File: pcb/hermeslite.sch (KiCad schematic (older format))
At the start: 68 parts, among them CN1 MEC6-140_CONNECTOR_BEMICRO, CN2 PCIE, P1 DIL20, P15 61.440, P16 DIPSW, P2 CONN_15, P24 BNC, P25 BNC, P3 CONN_1, P4 CONN_1, P5 CONN_1, P6 CONN_1, P7 CONN_1, T1 8:1, T3 4:1, U1 AD9866BCPZ

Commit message: RTL cleanup and upgrade to Quartus 14.0
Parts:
- C1, C10, C11, C12, C13, C14, C15, C16, C17, C18, C2, C21, C23, C24, C26, C27, C28, C29, C3, C30, C4, C5, C6, C7, C8, C9, R2, R3, R4, R5, R6, R7: footprint (none) -> SMD_Packages:SM0805
- C19, C20, C22: footprint (none) -> SMD_Packages:SM1206POL
- C25: footprint (none) -> SMD_Packages:SM1206
- C31, C32, R8, R9: footprint (none) -> SMD_Packages:SMD-0805
- CN1: footprint (none) -> HERMESLITE:MEC6-140-02-X-D-RAX
- CN2: footprint (none) -> HERMESLITE:PCIE36
- CN3: renamed from P1; footprint (none) -> HERMESLITE:WAVESHARE
- CN4: renamed from P2; footprint (none) -> HERMESLITE:SATA22
- D1: footprint (none) -> HERMESLITE:SOD323
- FB1: renamed from L1; footprint (none) -> SMD_Packages:SMD-0805
- FB2: renamed from L2; footprint (none) -> SMD_Packages:SMD-0805
- FB3: renamed from L3; footprint (none) -> SMD_Packages:SMD-0805
- FB4: renamed from L4; footprint (none) -> SMD_Packages:SMD-0805
- FB5: renamed from L5; footprint (none) -> SMD_Packages:SMD-0805
- J1: renamed from R10; footprint (none) -> SMD_Packages:SMD-0805
- J2: renamed from R11; footprint (none) -> SMD_Packages:SMD-0805
- J3: renamed from R14; value R -> 0; footprint (none) -> SMD_Packages:SMD-0805
- J4: renamed from R1; footprint (none) -> SMD_Packages:SMD-0805
- J5: renamed from R13; value R -> 0; footprint (none) -> SMD_Packages:SMD-0805
- P0: renamed from P5; footprint (none) -> Measurement_Points:Measurement_Point_Round-TH_Small
- P12: renamed from P4; footprint (none) -> Measurement_Points:Measurement_Point_Round-TH_Small
- P3: renamed from P7; footprint (none) -> Measurement_Points:Measurement_Point_Round-TH_Small
- P5: renamed from P6; footprint (none) -> Measurement_Points:Measurement_Point_Round-TH_Small
- PB3: renamed from P3; footprint (none) -> Measurement_Points:Measurement_Point_Round-TH_Small
- R1: renamed from R12; footprint (none) -> SMD_Packages:SM0805
- RX1: renamed from P25; footprint (none) -> HERMESLITE:BNCRA
- SW1: renamed from P16; footprint (none) -> HERMESLITE:DIPSWITCH
- T1: footprint (none) -> MINICKTS:minicircuits-CD542
- T2: renamed from T3; footprint (none) -> MINICKTS:minicircuits-CD542
- TX1: renamed from P24; footprint (none) -> HERMESLITE:BNCRA
- U1: footprint (none) -> HERMESLITE:CP_64_3-M
- renumbered P15 to X1

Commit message: Intermediate save before move of PCIe connector
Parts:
- removed CN3: DIL20, HERMESLITE:WAVESHARE, symbol DIL20
- removed CN4: CONN_15, HERMESLITE:SATA22, symbol CONN_15
- removed D1: CDSOD323, HERMESLITE:SOD323, symbol DIODESCH
- removed R3: 10K, SMD_Packages:SM0805, symbol R
- removed R7: 0, SMD_Packages:SM0805, symbol R
- removed R8, R9: 0, SMD_Packages:SMD-0805, symbol R
- removed SW1: DIPSW, HERMESLITE:DIPSWITCH, symbol dipswitch
- removed T2: 4:1, MINICKTS:minicircuits-CD542, symbol TRANSF_ADT2
- added C33: 0.1UF, SMD_Packages:SMD-0805, symbol Csmall
- added CN4: SATA22, HERMESLITE:SATA22, symbol SATA22
- added D1: CDSOD323, HERMESLITE:SOD323, symbol DIODESCH2
- added T2: 4:1, HERMESLITE:TRANSF, symbol TRANSF
- added TP1, TP2: CONN_1, HERMESLITE:TP, symbol CONN_1
- added U2: EEPROM, SMD_Packages:SOT-23-6, symbol EEPROM
- C1, C10, C11, C12, C13, C14, C15, C16, C17, C18, C2, C21, C23, C24, C26, C27, C28, C29, C3, C30, C4, C5, C6, C7, C8, C9, R1, R2: footprint SMD_Packages:SM0805 -> SMD_Packages:SMD-0805
- C19, C20, C22: footprint SMD_Packages:SM1206POL -> SMD_Packages:SMD-1206_Pol
- C25: footprint SMD_Packages:SM1206 -> SMD_Packages:SMD-1206
- CN2: footprint HERMESLITE:PCIE36 -> HERMESLITE:PCIESTRADDLE
- R3: renamed from R6; footprint SMD_Packages:SM0805 -> SMD_Packages:SMD-0805
- R4, R5: value 10K -> 47; footprint SMD_Packages:SM0805 -> SMD_Packages:SMD-0805
- RX1, TX1: value BNC -> ~; footprint HERMESLITE:BNCRA -> HERMESLITE:RFSTRADDLE
- T1: footprint MINICKTS:minicircuits-CD542 -> HERMESLITE:TRANSF
- X1: footprint (none) -> HERMESLITE:Si510
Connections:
- wire segments 298 -> 269
- no-connect marks 5 -> 11
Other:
- moved on the sheet: C21, C22, C26, C27, C30, FB5, J5, P0, P12, P3, P5, R3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

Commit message: Commit before silkscreen cleanup
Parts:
- removed C22: 10UF, SMD_Packages:SMD-1206_Pol, symbol CPsmall
- removed D1: CDSOD323, HERMESLITE:SOD323, symbol DIODESCH2
- removed R3: 0, SMD_Packages:SMD-0805, symbol R
- removed RX1, TX1: ~, HERMESLITE:RFSTRADDLE, symbol BNC
- removed T1: 8:1, HERMESLITE:TRANSF, symbol TRANSF
- removed T2: 4:1, HERMESLITE:TRANSF, symbol TRANSF
- added C22, C34, C35, C36: 0.1UF, SMD_Packages:SMD-0805, symbol Csmall
- added FB6, FB7, FB8: FB, SMD_Packages:SMD-0805, symbol FB
- added R6: 200, SMD_Packages:SMD-0805, symbol R
- C17, C18: symbol CPsmall -> Csmall
- C21, C26, C27, C30: value 0.1UF -> 1UF
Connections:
- net labels added: EXP12V, EXP3V, EXP5V, EXP_GPIO0, EXP_GPIO1, EXP_GPIO2, EXP_SCLK, EXP_SDI, EXP_SDO, EXP_SEN, FPGA5V, PTT#
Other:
- moved on the sheet: C1, C10, C11, C12, C13, C14, C2, C3, C4, C5, C6, C7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

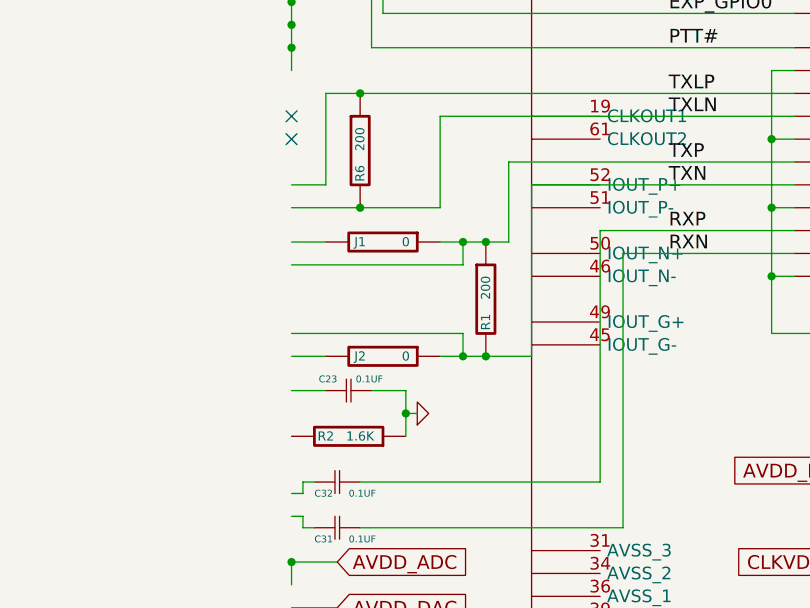
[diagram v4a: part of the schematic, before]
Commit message: Updated BOM, renumbered a few references
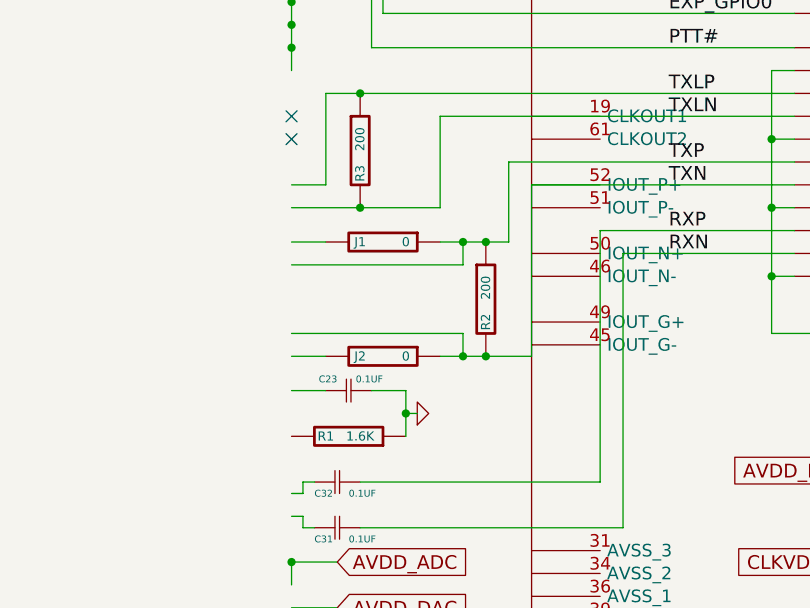
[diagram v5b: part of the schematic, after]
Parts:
- renumbered CN4 to CN3, R2 to R1, R1 to R2, R6 to R3
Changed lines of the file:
@@
 Sheet 1 1
 Title "Hermes-Lite"
-Date "05 Oct 2014"
+Date "07 Oct 2014"
 Rev "1.2"
 Comp "SofterHardware"
@@
 $EndComp
 $Comp
-L R R2
+L R R1
 U 1 1 52CF8B35
 P 6700 4850
-F 0 "R2" V 6700 4750 40  0000 C CNN
+F 0 "R1" V 6700 4750 40  0000 C CNN
 F 1 "1.6K" V 6700 4900 40  0000 C CNN
 F 2 "SMD_Packages:SMD-0805" V 6630 4850 30  0001 C CNN
@@
 12VIN
 $Comp
-L R R1
+L R R2
 U 1 1 53FA8C29
 P 7300 4250
-F 0 "R1" V 7300 4150 40  0000 C CNN
+F 0 "R2" V 7300 4150 40  0000 C CNN
 F 1 "200" V 7300 4300 40  0000 C CNN
 F 2 "SMD_Packages:SMD-0805" V 7230 4250 30  0001 C CNN
@@
 $EndComp
 $Comp
-L SATA22 CN4
+L SATA22 CN3
 U 1 1 5420EEBF
 P 3300 7500
-F 0 "CN4" V 3350 9050 60  0000 C CNN
+F 0 "CN3" V 3350 9050 60  0000 C CNN
 F 1 "SATA22" V 3350 7050 60  0000 C CNN
 F 2 "HERMESLITE:SATA22" H 3300 7500 60  0001 C CNN
@@
 	2100 6800 2100 7150
 $Comp
-L R R6
+L R R3
 U 1 1 542B8A14
 P 6750 3600
-F 0 "R6" V 6750 3500 40  0000 C CNN
+F 0 "R3" V 6750 3500 40  0000 C CNN
 F 1 "200" V 6750 3650 40  0000 C CNN
 F 2 "SMD_Packages:SMD-0805" V 6680 3600 30  0001 C CNN

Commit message: iTead Studio submission
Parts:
- U2: footprint SMD_Packages:SOT-23-6 -> MODULE
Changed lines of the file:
@@
 Sheet 1 1
 Title "Hermes-Lite"
-Date "07 Oct 2014"
+Date "08 Oct 2014"
 Rev "1.2"
 Comp "SofterHardware"
@@
 	1    1600 7050
 	0    1    1    0
-$EndComp
-$Comp
-L EEPROM U2
-U 1 1 5421E05F
-P 1150 4350
-F 0 "U2" V 1300 4550 50  0000 C CNN
-F 1 "EEPROM" H 1000 4725 50  0001 C CNN
-F 2 "SMD_Packages:SOT-23-6" H 1150 3875 50  0001 C CNN
-F 3 "DOCUMENTATION" H 1125 3950 50  0001 C CNN
-	1    1150 4350
-	0    -1   -1   0
 $EndComp
 NoConn ~ 1550 4400
@@
 	1750 750  1700 750
 Connection ~ 1350 750
+$Comp
+L EEPROM U2
+U 1 1 54362814
+P 1150 4350
+F 0 "U2" V 1300 4550 50  0000 C CNN
+F 1 "EEPROM" H 1000 4725 50  0001 C CNN
+F 2 "MODULE" H 1150 3875 50  0001 C CNN
+F 3 "DOCUMENTATION" H 1125 3950 50  0001 C CNN
+	1    1150 4350
+	0    -1   -1   0
+$EndComp
 $EndSCHEMATC

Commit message: Added revision 1.21
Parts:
- removed CN3: SATA22, HERMESLITE:SATA22, symbol SATA22
- removed PB3: CONN_1, Measurement_Points:Measurement_Point_Round-TH_Small, symbol CONN_1
- added CN3: GPIO, HERMESLITE:EDGE6, symbol EDGECONN_6X2
- added CN4: POWER, HERMESLITE:EDGE6, symbol EDGECONN_6X2
- added J6: 0, SMD_Packages:SMD-0805, symbol R
- added J7, J8: 0, HERMESLITE:JUMPER, symbol R
- added P1: CONN_1, symbol CONN_1
- added Palt0, S1, S2, S3: CONN_1, Measurement_Points:Measurement_Point_Round-TH_Small, symbol CONN_1
- added TP3, TP4, TP5, TP6: CONN_1, HERMESLITE:TP, symbol CONN_1
- J5: footprint SMD_Packages:SMD-0805 -> HERMESLITE:JUMPER
- U2: footprint MODULE -> SMD_Packages:SOT-23-6
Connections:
- net labels added: MCSn, MSCK, MSI, MSO
- wire segments 269 -> 302
- no-connect marks 11 -> 2
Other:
- moved on the sheet: C33, J4, J5, P0, P12, P3, P5

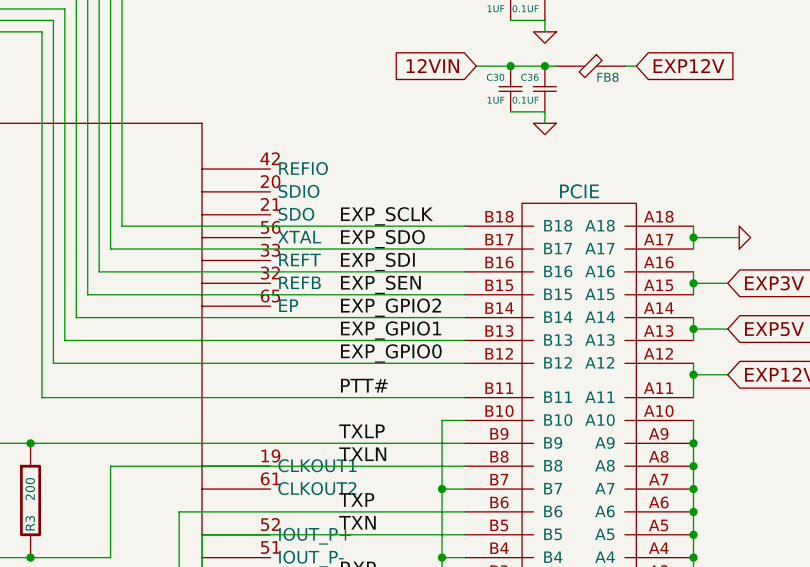
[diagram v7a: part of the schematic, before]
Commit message: Updated schematics for user[6:0]
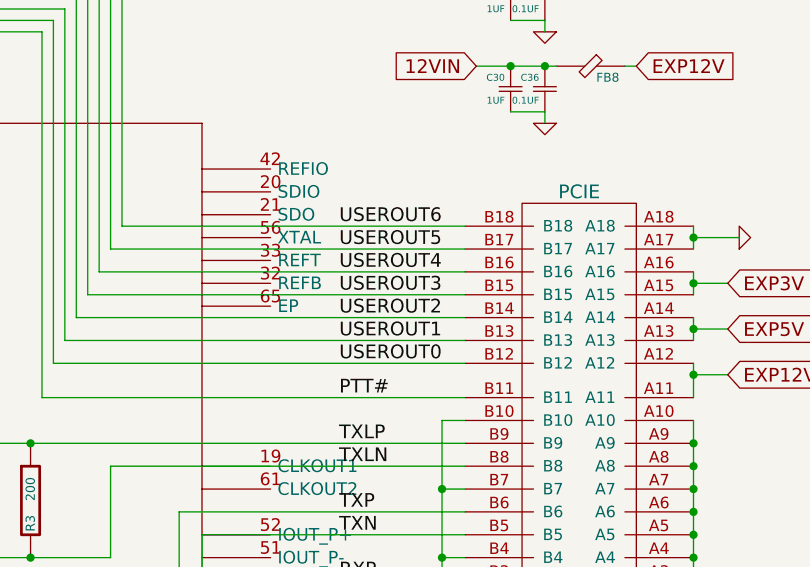
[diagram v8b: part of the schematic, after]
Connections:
- net labels added: USEROUT0, USEROUT1, USEROUT2, USEROUT3, USEROUT4, USEROUT5, USEROUT6
- net labels removed: EXP_GPIO0, EXP_GPIO1, EXP_GPIO2, EXP_SCLK, EXP_SDI, EXP_SDO, EXP_SEN
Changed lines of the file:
@@
 RXN
 Text Label 8100 2400 0    60   ~ 0
-EXP_SCLK
+USEROUT6
 Text Label 8100 2500 0    60   ~ 0
-EXP_SDO
+USEROUT5
 Text Label 8100 2600 0    60   ~ 0
-EXP_SDI
+USEROUT4
 Text Label 8100 2700 0    60   ~ 0
-EXP_SEN
+USEROUT3
 Text Label 8100 3150 0    60   ~ 0
 PTT#
 Text Label 8100 2800 0    60   ~ 0
-EXP_GPIO2
+USEROUT2
 Text Label 8100 2900 0    60   ~ 0
-EXP_GPIO1
+USEROUT1
 Text Label 8100 3000 0    60   ~ 0
-EXP_GPIO0
+USEROUT0
 $Comp
 L GND #PWR015
